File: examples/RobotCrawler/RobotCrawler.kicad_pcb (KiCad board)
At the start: 2 copper layers, 50 x 40 mm, 55 parts

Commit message: floorplanned
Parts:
- removed rgb_tp: 5015 (Keystone) - _mcu_gpio_rgb_link, edg:TestPoint_TE_RCT_0805
- removed tp_1v2: 5015 (Keystone) - v1v2, edg:TestPoint_TE_RCT_0805
- removed tp_2v5: 5015 (Keystone) - v2v5, edg:TestPoint_TE_RCT_0805
- moved reg_2v5.ic 140.7 mm to (163.0, 65.0)
- moved reg_2v5.in_cap 140.7 mm to (163.0, 62.0)
- moved reg_2v5.out_cap 140.7 mm to (163.0, 68.0)
- moved rgbs.led[3] 122.8 mm to (163.0, 76.0)
- moved rgbs.led[2] 122.6 mm to (163.0, 72.0)
- moved cam.reset_pull 120.2 mm to (156.0, 73.0), turned to 90 degrees
- moved reg_1v2.ic 116.7 mm to (137.0, 65.0)
- moved reg_1v2.in_cap 116.7 mm to (137.0, 62.0)
- moved reg_1v2.out_cap 116.7 mm to (137.0, 68.0)
- moved cam.dovdd_cap 116.6 mm to (150.0, 73.0), turned to -90 degrees
- moved cam.pclk_cap 116.6 mm to (147.0, 73.0), turned to -90 degrees
- moved cam.reset_cap 116.6 mm to (153.0, 73.0), turned to -90 degrees
- moved cam.device 115.1 mm to (150.0, 64.0)
- moved rgbs.led[0] 100.8 mm to (137.0, 76.0)
- moved rgbs.led[1] 98.4 mm to (137.0, 72.0)
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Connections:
- net rgb_tp.io renamed rgbs.din
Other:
- board size 50 x 40 mm -> 50 x 50 mm

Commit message: wip
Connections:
- mcu.ic pad 10: cam.y.9 -> i2c_chain_0.scl
- mcu.ic pad 11: cam.pclk -> servo4.pwm
- mcu.ic pad 12: ledg.signal -> servo3.pwm
- mcu.ic pad 13: cam.xclk -> cam.vsync
- mcu.ic pad 15: servo3.fb -> cam.y.9
- mcu.ic pad 17: ledb.signal -> cam.xclk
- mcu.ic pad 18: cam.y.2 -> cam.y.8
- mcu.ic pad 19: cam.y.3 -> cam.y.7
- mcu.ic pad 20: cam.y.4 -> cam.pclk
- mcu.ic pad 21: cam.y.5 -> cam.y.6
- mcu.ic pad 22: cam.y.6 -> cam.y.2
- mcu.ic pad 23: cam.vsync -> cam.y.5
- mcu.ic pad 24: servo2.pwm -> cam.y.3
- mcu.ic pad 25: servo1.pwm -> cam.y.4
- mcu.ic pad 31: servo3.pwm -> servo1.pwm
- mcu.ic pad 32: servo4.pwm -> servo2.pwm
- mcu.ic pad 33: rgbs.din -> ledr.signal
- mcu.ic pad 34: (no net) -> ledg.signal
- mcu.ic pad 35: (no net) -> ledb.signal
- mcu.ic pad 38: servo2.fb -> rgbs.din
- mcu.ic pad 39: servo1.fb -> (no net)
- mcu.ic pad 4: servo4.fb -> servo1.fb
- mcu.ic pad 5: i2c_chain_0.scl -> servo2.fb
- mcu.ic pad 6: i2c_chain_0.sda -> servo3.fb
- mcu.ic pad 7: ledr.signal -> servo4.fb
- mcu.ic pad 8: cam.y.7 -> (no net)
- mcu.ic pad 9: cam.y.8 -> i2c_chain_0.sda
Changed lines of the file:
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@@
       (net 11 "mcu.program_en_node"))
     (pad "4" smd rect (at -8.75 -1.45 180) (size 1.5 0.9) (layers "F.Cu" "F.Paste" "F.Mask")
+      (net 38 "servo1.fb"))
+    (pad "5" smd rect (at -8.75 -0.18 180) (size 1.5 0.9) (layers "F.Cu" "F.Paste" "F.Mask")
+      (net 37 "servo2.fb"))
+    (pad "6" smd rect (at -8.75 1.09 180) (size 1.5 0.9) (layers "F.Cu" "F.Paste" "F.Mask")
+      (net 22 "servo3.fb"))
+    (pad "7" smd rect (at -8.75 2.36 180) (size 1.5 0.9) (layers "F.Cu" "F.Paste" "F.Mask")
       (net 13 "servo4.fb"))
-    (pad "5" smd rect (at -8.75 -0.18 180) (size 1.5 0.9) (layers "F.Cu" "F.Paste" "F.Mask")
+    (pad "8" smd rect (at -8.75 3.63 180) (size 1.5 0.9) (layers "F.Cu" "F.Paste" "F.Mask"))
+    (pad "9" smd rect (at -8.75 4.9 180) (size 1.5 0.9) (layers "F.Cu" "F.Paste" "F.Mask")
+      (net 3 "i2c_chain_0.sda"))
+    (pad "10" smd rect (at -8.75 6.17 180) (size 1.5 0.9) (layers "F.Cu" "F.Paste" "F.Mask")
       (net 5 "i2c_chain_0.scl"))
-    (pad "6" smd rect (at -8.75 1.09 180) (size 1.5 0.9) (layers "F.Cu" "F.Paste" "F.Mask")
-      (net 3 "i2c_chain_0.sda"))
-    (pad "7" smd rect (at -8.75 2.36 180) (size 1.5 0.9) (layers "F.Cu" "F.Paste" "F.Mask")
-      (net 14 "ledr.signal"))
-    (pad "8" smd rect (at -8.75 3.63 180) (size 1.5 0.9) (layers "F.Cu" "F.Paste" "F.Mask")
-      (net 15 "cam.y.7"))
-    (pad "9" smd rect (at -8.75 4.9 180) (size 1.5 0.9) (layers "F.Cu" "F.Paste" "F.Mask")
-      (net 16 "cam.y.8"))
-    (pad "10" smd rect (at -8.75 6.17 180) (size 1.5 0.9) (layers "F.Cu" "F.Paste" "F.Mask")
-      (net 17 "cam.y.9"))
     (pad "11" smd rect (at -8.75 7.44 180) (size 1.5 0.9) (layers "F.Cu" "F.Paste" "F.Mask")
-      (net 18 "cam.pclk"))
+      (net 34 "servo4.pwm"))
     (pad "12" smd rect (at -8.75 8.71 180) (size 1.5 0.9) (layers "F.Cu" "F.Paste" "F.Mask")
-      (net 19 "ledg.signal"))
+      (net 33 "servo3.pwm"))
     (pad "13" smd rect (at -8.75 9.98 180) (size 1.5 0.9) (layers "F.Cu" "F.Paste" "F.Mask")
-      (net 20 "cam.xclk"))
+      (net 29 "cam.vsync"))
     (pad "14" smd rect (at -8.75 11.25) (size 1.5 0.9) (layers "F.Cu" "F.Paste" "F.Mask")
       (net 21 "cam.href"))
     (pad "15" smd rect (at -6.985 12.5 90) (size 1.5 0.9) (layers "F.Cu" "F.Paste" "F.Mask")
-      (net 22 "servo3.fb"))
+      (net 17 "cam.y.9"))
     (pad "16" smd rect (at -5.715 12.5 90) (size 1.5 0.9) (layers "F.Cu" "F.Paste" "F.Mask"))
     (pad "17" smd rect (at -4.445 12.5 90) (size 1.5 0.9) (layers "F.Cu" "F.Paste" "F.Mask")
-      (net 23 "ledb.signal"))
+      (net 20 "cam.xclk"))
     (pad "18" smd rect (at -3.175 12.5 90) (size 1.5 0.9) (layers "F.Cu" "F.Paste" "F.Mask")
+      (net 16 "cam.y.8"))
+    (pad "19" smd rect (at -1.905 12.5 90) (size 1.5 0.9) (layers "F.Cu" "F.Paste" "F.Mask")
+      (net 15 "cam.y.7"))
+    (pad "20" smd rect (at -0.635 12.5 90) (size 1.5 0.9) (layers "F.Cu" "F.Paste" "F.Mask")
+      (net 18 "cam.pclk"))
+    (pad "21" smd rect (at 0.635 12.5 90) (size 1.5 0.9) (layers "F.Cu" "F.Paste" "F.Mask")
+      (net 28 "cam.y.6"))
+    (pad "22" smd rect (at 1.905 12.5 90) (size 1.5 0.9) (layers "F.Cu" "F.Paste" "F.Mask")
       (net 24 "cam.y.2"))
-    (pad "19" smd rect (at -1.905 12.5 90) (size 1.5 0.9) (layers "F.Cu" "F.Paste" "F.Mask")
+    (pad "23" smd rect (at 3.175 12.5 90) (size 1.5 0.9) (layers "F.Cu" "F.Paste" "F.Mask")
+      (net 27 "cam.y.5"))
+    (pad "24" smd rect (at 4.445 12.5 90) (size 1.5 0.9) (layers "F.Cu" "F.Paste" "F.Mask")
       (net 25 "cam.y.3"))
-    (pad "20" smd rect (at -0.635 12.5 90) (size 1.5 0.9) (layers "F.Cu" "F.Paste" "F.Mask")
+    (pad "25" smd rect (at 5.715 12.5 90) (size 1.5 0.9) (layers "F.Cu" "F.Paste" "F.Mask")
       (net 26 "cam.y.4"))
-    (pad "21" smd rect (at 0.635 12.5 90) (size 1.5 0.9) (layers "F.Cu" "F.Paste" "F.Mask")
-      (net 27 "cam.y.5"))
-    (pad "22" smd rect (at 1.905 12.5 90) (size 1.5 0.9) (layers "F.Cu" "F.Paste" "F.Mask")
-      (net 28 "cam.y.6"))
-    (pad "23" smd rect (at 3.175 12.5 90) (size 1.5 0.9) (layers "F.Cu" "F.Paste" "F.Mask")
-      (net 29 "cam.vsync"))
-    (pad "24" smd rect (at 4.445 12.5 90) (size 1.5 0.9) (layers "F.Cu" "F.Paste" "F.Mask")
-      (net 30 "servo2.pwm"))
-    (pad "25" smd rect (at 5.715 12.5 90) (size 1.5 0.9) (layers "F.Cu" "F.Paste" "F.Mask")
-      (net 31 "servo1.pwm"))
     (pad "26" smd rect (at 6.985 12.5 90) (size 1.5 0.9) (layers "F.Cu" "F.Paste" "F.Mask"))
     (pad "27" smd rect (at 8.75 11.25 180) (size 1.5 0.9) (layers "F.Cu" "F.Paste" "F.Mask")
@@
     (pad "30" smd rect (at 8.75 7.44 180) (size 1.5 0.9) (layers "F.Cu" "F.Paste" "F.Mask"))
     (pad "31" smd rect (at 8.75 6.17 180) (size 1.5 0.9) (layers "F.Cu" "F.Paste" "F.Mask")
-      (net 33 "servo3.pwm"))
+      (net 31 "servo1.pwm"))
     (pad "32" smd rect (at 8.75 4.9 180) (size 1.5 0.9) (layers "F.Cu" "F.Paste" "F.Mask")
-      (net 34 "servo4.pwm"))
+      (net 30 "servo2.pwm"))
     (pad "33" smd rect (at 8.75 3.63 180) (size 1.5 0.9) (layers "F.Cu" "F.Paste" "F.Mask")
-      (net 51 "rgbs.din"))
-    (pad "34" smd rect (at 8.75 2.36 180) (size 1.5 0.9) (layers "F.Cu" "F.Paste" "F.Mask"))
-    (pad "35" smd rect (at 8.75 1.09 180) (size 1.5 0.9) (layers "F.Cu" "F.Paste" "F.Mask"))
+      (net 14 "ledr.signal"))
+    (pad "34" smd rect (at 8.75 2.36 180) (size 1.5 0.9) (layers "F.Cu" "F.Paste" "F.Mask")
+      (net 19 "ledg.signal"))
+    (pad "35" smd rect (at 8.75 1.09 180) (size 1.5 0.9) (layers "F.Cu" "F.Paste" "F.Mask")
+      (net 23 "ledb.signal"))
     (pad "36" smd rect (at 8.75 -0.18 180) (size 1.5 0.9) (layers "F.Cu" "F.Paste" "F.Mask")
       (net 35 "mcu.program_uart_node.b_tx"))
@@
       (net 36 "mcu.program_uart_node.a_tx"))
     (pad "38" smd rect (at 8.75 -2.72 180) (size 1.5 0.9) (layers "F.Cu" "F.Paste" "F.Mask")
-      (net 37 "servo2.fb"))
-    (pad "39" smd rect (at 8.75 -3.99 180) (size 1.5 0.9) (layers "F.Cu" "F.Paste" "F.Mask")
-      (net 38 "servo1.fb"))
+      (net 51 "rgbs.din"))
+    (pad "39" smd rect (at 8.75 -3.99 180) (size 1.5 0.9) (layers "F.Cu" "F.Paste" "F.Mask"))
     (pad "40" smd rect (at 8.75 -5.26 180) (size 1.5 0.9) (layers "F.Cu" "F.Paste" "F.Mask")
       (net 1 "gnd"))

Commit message: improvements to help routing
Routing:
- net mcu.program_uart_node.b_tx: track 0.00 -> 3.78 mm
- net mcu.program_uart_node.a_tx: track 0.00 -> 3.78 mm
- net gnd: track 0.00 -> 2.99 mm
- net v3v3: track 0.00 -> 2.88 mm
- net mcu.program_boot_node: track 0.00 -> 2.88 mm
- net mcu.program_en_node: track 0.00 -> 2.84 mm
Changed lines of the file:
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@@
     (fp_arc (start 0.62074 1.407352) (mid 0.5 1.499999) (end 0.37926 1.407352)
       (stroke (width 0.16) (type solid)) (layer "B.Cu"))
-    (fp_arc (start 0.763205 0.913443) (mid 0.969128 0.866757) (end 1.178844 0.891296)
+    (fp_arc (start 0.763205 0.913443) (mid 0.969127 0.866756) (end 1.178844 0.891296)
       (stroke (width 0.16) (type solid)) (layer "B.Cu"))
     (fp_arc (start 0.820058 -1.56145) (mid 0.75756 -1.62395) (end 0.820058 -1.68645)
@@
     (fp_arc (start 0.820058 -1.43645) (mid 0.75756 -1.49895) (end 0.820058 -1.56145)
       (stroke (width 0.16) (type solid)) (layer "B.Cu"))
-    (fp_arc (start 0.869178 1.169286) (mid 1.000175 1.003685) (end 1.178836 0.891151)
+    (fp_arc (start 0.869178 1.169286) (mid 1.000175 1.003686) (end 1.178836 0.891151)
       (stroke (width 0.16) (type solid)) (layer "B.Cu"))
     (fp_arc (start 1.093749 -1.89443) (mid 0.000001 2.187499) (end -1.09375 -1.894429)
@@
     (style (thickness 0.1) (arrow_length 1.27) (text_position_mode 0) (extension_height 0.58642) (extension_offset 0.5) keep_text_aligned)
   )
+  (segment (start 135 106.905) (end 135 109) (width 0.3) (layer "F.Cu") (net 1))
+  (segment (start 134.365 106.27) (end 135 106.905) (width 0.3) (layer "F.Cu") (net 1))
+  (segment (start 135.635 106.27) (end 136.030416 106.27) (width 0.15) (layer "F.Cu") (net 11))
+  (segment (start 136.030416 106.27) (end 137.760416 108) (width 0.15) (layer "F.Cu") (net 11))
+  (segment (start 134.365 103.73) (end 134.1007 103.4657) (width 0.3) (layer "F.Cu") (net 12))
+  (segment (start 134.1007 101.1007) (end 134 101) (width 0.3) (layer "F.Cu") (net 12))
+  (segment (start 134.1007 103.4657) (end 134.1007 101.1007) (width 0.3) (layer "F.Cu") (net 12))
+  (segment (start 136 103.365) (end 136 101) (width 0.15) (layer "F.Cu") (net 32))
+  (segment (start 135.635 103.73) (end 136 103.365) (width 0.15) (layer "F.Cu") (net 32))
+  (segment (start 136.635 104) (end 139 104) (width 0.15) (layer "F.Cu") (net 35))
+  (segment (start 135.635 105) (end 136.635 104) (width 0.15) (layer "F.Cu") (net 35))
+  (segment (start 134.365 105) (end 133.365 104) (width 0.15) (layer "F.Cu") (net 36))
+  (segment (start 133.365 104) (end 131 104) (width 0.15) (layer "F.Cu") (net 36))
   (zone (net 1) (net_name "gnd") (layers "F&B.Cu") (hatch edge 0.508)
     (connect_pads (clearance 0.254))

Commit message: Update RobotCrawler.kicad_pcb
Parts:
- moved cam.device 18.0 mm to (150.0, 82.0)
- moved reg_2v5.in_cap 15.7 mm to (156.0, 76.0), turned to -90 degrees
- moved rgbs.led[0] 14.6 mm to (141.0, 62.0)
- moved rgbs.led[3] 14.6 mm to (159.0, 62.0)
- moved rgbs.led[1] 14.1 mm to (147.0, 62.0)
- moved rgbs.led[2] 14.1 mm to (153.0, 62.0)
- moved reg_1v2.in_cap 14.0 mm to (138.0, 76.0), turned to 90 degrees
- moved compass.c1 14.0 mm to (155.0, 67.0)
- moved compass.ic 14.0 mm to (150.0, 66.0)
- moved compass.set_cap 14.0 mm to (155.0, 65.0)
- moved compass.vdd_cap 14.0 mm to (145.0, 65.0)
- moved i2c_pull.scl_res 14.0 mm to (145.0, 67.0)
- moved i2c_pull.sda_res 14.0 mm to (145.0, 69.0)
- moved imu.ic 14.0 mm to (150.0, 71.0)
- moved imu.vdd_cap 14.0 mm to (155.0, 71.0)
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
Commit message: layout round 2
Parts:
- turned C10 to -90 degrees
- turned C15 to 90 degrees
- turned C16 to 90 degrees
- turned C17 to 90 degrees
- turned R7 to -90 degrees
- renumbered imu.vdd_cap to C1, reg_1v2.in_cap to C10, reg_1v2.out_cap to C11, mcu.vcc_cap0 to C12, mcu.vcc_cap1 to C13, mcu.en_pull.c to C14, cam.dovdd_cap to C15, cam.pclk_cap to C16, cam.reset_cap to C17, imu.vddio_cap to C2, compass.vdd_cap to C3, compass.set_cap to C4, compass.c1 to C5, reg_3v3.in_cap to C6, reg_3v3.out_cap to C7, reg_2v5.in_cap to C8, reg_2v5.out_cap to C9, ledr.package to D1, ledg.package to D2, ledb.package to D3, rgbs.led[0] to D4, rgbs.led[1] to D5, rgbs.led[2] to D6, rgbs.led[3] to D7, batt to J1, servo1 to J2, servo2 to J3, servo3 to J4, servo4 to J5, mcu.prog to J6, cam.device to J7, mcu.en_pull.r to R1, i2c_pull.scl_res to R2, i2c_pull.sda_res to R3, ledr.res to R4, ledg.res to R5, ledb.res to R6, cam.reset_pull to R7, tp_vbatt to TP1, tp_gnd to TP2, tp_3v3 to TP3, i2c_tp.tp_scl to TP4, i2c_tp.tp_sda to TP5, imu.ic to U1, compass.ic to U2, reg_3v3.ic to U3, reg_2v5.ic to U4, reg_1v2.ic to U5, mcu.ic to U6

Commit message: Update RobotCrawler.kicad_pcb
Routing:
- net mcu.program_uart_node.a_tx: track 3.78 -> 0.00 mm
- net mcu.program_en_node: track 2.84 -> 0.00 mm
- net gnd: track 2.99 -> 2.05 mm
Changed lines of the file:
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@@
     (fp_arc (start 0.62074 1.407352) (mid 0.5 1.499999) (end 0.37926 1.407352)
       (stroke (width 0.16) (type solid)) (layer "B.Cu"))
-    (fp_arc (start 0.763205 0.913443) (mid 0.969127 0.866758) (end 1.178844 0.891296)
+    (fp_arc (start 0.763205 0.913443) (mid 0.969128 0.866757) (end 1.178844 0.891296)
       (stroke (width 0.16) (type solid)) (layer "B.Cu"))
     (fp_arc (start 0.820058 -1.56145) (mid 0.75756 -1.62395) (end 0.820058 -1.68645)
@@
     (fp_arc (start 0.820058 -1.43645) (mid 0.75756 -1.49895) (end 0.820058 -1.56145)
       (stroke (width 0.16) (type solid)) (layer "B.Cu"))
-    (fp_arc (start 0.869178 1.169286) (mid 1.000176 1.003686) (end 1.178836 0.891151)
+    (fp_arc (start 0.869178 1.169286) (mid 1.000175 1.003684) (end 1.178836 0.891151)
       (stroke (width 0.16) (type solid)) (layer "B.Cu"))
     (fp_arc (start 1.093749 -1.89443) (mid 0.000001 2.187499) (end -1.09375 -1.894429)
@@
     (style (thickness 0.1) (arrow_length 1.27) (text_position_mode 0) (extension_height 0.58642) (extension_offset 0.5) keep_text_aligned)
   )
-  (segment (start 135 106.905) (end 135 109) (width 0.3) (layer "F.Cu") (net 1))
-  (segment (start 134.365 106.27) (end 135 106.905) (width 0.3) (layer "F.Cu") (net 1))
-  (segment (start 135.635 106.27) (end 136.030416 106.27) (width 0.15) (layer "F.Cu") (net 11))
-  (segment (start 136.030416 106.27) (end 137.760416 108) (width 0.15) (layer "F.Cu") (net 11))
+  (segment (start 134.052908 106.27) (end 132.822908 107.5) (width 0.2) (layer "F.Cu") (net 1))
+  (segment (start 134.365 106.27) (end 134.052908 106.27) (width 0.2) (layer "F.Cu") (net 1))
   (segment (start 134.365 103.73) (end 134.1007 103.4657) (width 0.3) (layer "F.Cu") (net 12))
-  (segment (start 134.1007 101.1007) (end 134 101) (width 0.3) (layer "F.Cu") (net 12))
   (segment (start 134.1007 103.4657) (end 134.1007 101.1007) (width 0.3) (layer "F.Cu") (net 12))
   (segment (start 136 103.365) (end 136 101) (width 0.15) (layer "F.Cu") (net 32))
@@
   (segment (start 136.635 104) (end 139 104) (width 0.15) (layer "F.Cu") (net 35))
   (segment (start 135.635 105) (end 136.635 104) (width 0.15) (layer "F.Cu") (net 35))
-  (segment (start 134.365 105) (end 133.365 104) (width 0.15) (layer "F.Cu") (net 36))
-  (segment (start 133.365 104) (end 131 104) (width 0.15) (layer "F.Cu") (net 36))
   (zone (net 1) (net_name "gnd") (layers "F&B.Cu") (hatch edge 0.508)
     (connect_pads (clearance 0.254))

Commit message: Update RobotCrawler.kicad_pcb
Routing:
- net mcu.program_uart_node.a_tx: track 0.00 -> 9.75 mm, vias 0 -> 2
- net mcu.program_uart_node.b_tx: track 3.78 -> 6.01 mm
- net gnd: track 2.05 -> 2.37 mm, vias 0 -> 1
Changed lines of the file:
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@@
   (segment (start 134.052908 106.27) (end 132.822908 107.5) (width 0.2) (layer "F.Cu") (net 1))
   (segment (start 134.365 106.27) (end 134.052908 106.27) (width 0.2) (layer "F.Cu") (net 1))
+  (segment (start 132.822908 107.5) (end 132.5 107.5) (width 0.3) (layer "F.Cu") (net 1))
+  (via (at 132.5 107.5) (size 0.7) (drill 0.3) (layers "F.Cu" "B.Cu") (net 1))
   (segment (start 134.365 103.73) (end 134.1007 103.4657) (width 0.3) (layer "F.Cu") (net 12))
   (segment (start 134.1007 103.4657) (end 134.1007 101.1007) (width 0.3) (layer "F.Cu") (net 12))
   (segment (start 136 103.365) (end 136 101) (width 0.15) (layer "F.Cu") (net 32))
   (segment (start 135.635 103.73) (end 136 103.365) (width 0.15) (layer "F.Cu") (net 32))
-  (segment (start 136.635 104) (end 139 104) (width 0.15) (layer "F.Cu") (net 35))
-  (segment (start 135.635 105) (end 136.635 104) (width 0.15) (layer "F.Cu") (net 35))
+  (segment (start 136.51645 104.11855) (end 136.0675 104.5675) (width 0.15) (layer "F.Cu") (net 35))
+  (segment (start 141.25 104.18) (end 141.18855 104.11855) (width 0.15) (layer "F.Cu") (net 35))
+  (segment (start 141.18855 104.11855) (end 136.51645 104.11855) (width 0.15) (layer "F.Cu") (net 35))
+  (segment (start 135.635 105) (end 136.0675 104.5675) (width 0.15) (layer "F.Cu") (net 35))
+  (segment (start 134.365 105) (end 134.365 104.865) (width 0.15) (layer "F.Cu") (net 36))
+  (segment (start 134.365 104.865) (end 133.5 104) (width 0.15) (layer "F.Cu") (net 36))
+  (segment (start 140.05 105.45) (end 140 105.5) (width 0.15) (layer "F.Cu") (net 36))
+  (segment (start 141.25 105.45) (end 140.05 105.45) (width 0.15) (layer "F.Cu") (net 36))
+  (via (at 140 105.5) (size 0.7) (drill 0.3) (layers "F.Cu" "B.Cu") (net 36))
+  (via (at 133.5 104) (size 0.7) (drill 0.3) (layers "F.Cu" "B.Cu") (net 36))
+  (segment (start 133.5 104) (end 138.5 104) (width 0.15) (layer "B.Cu") (net 36))
+  (segment (start 138.5 104) (end 140 105.5) (width 0.15) (layer "B.Cu") (net 36))
   (zone (net 1) (net_name "gnd") (layers "F&B.Cu") (hatch edge 0.508)
     (connect_pads (clearance 0.254))
@@
     (polygon
       (pts
-        (xy 175.5 110.5)
-        (xy 124.5 110.5)
-        (xy 124.5 59.5)
-        (xy 175.5 59.5)
+        (xy 123.5 110)
+        (xy 72.5 110)
+        (xy 72.5 59)
+        (xy 123.5 59)
       )
     )

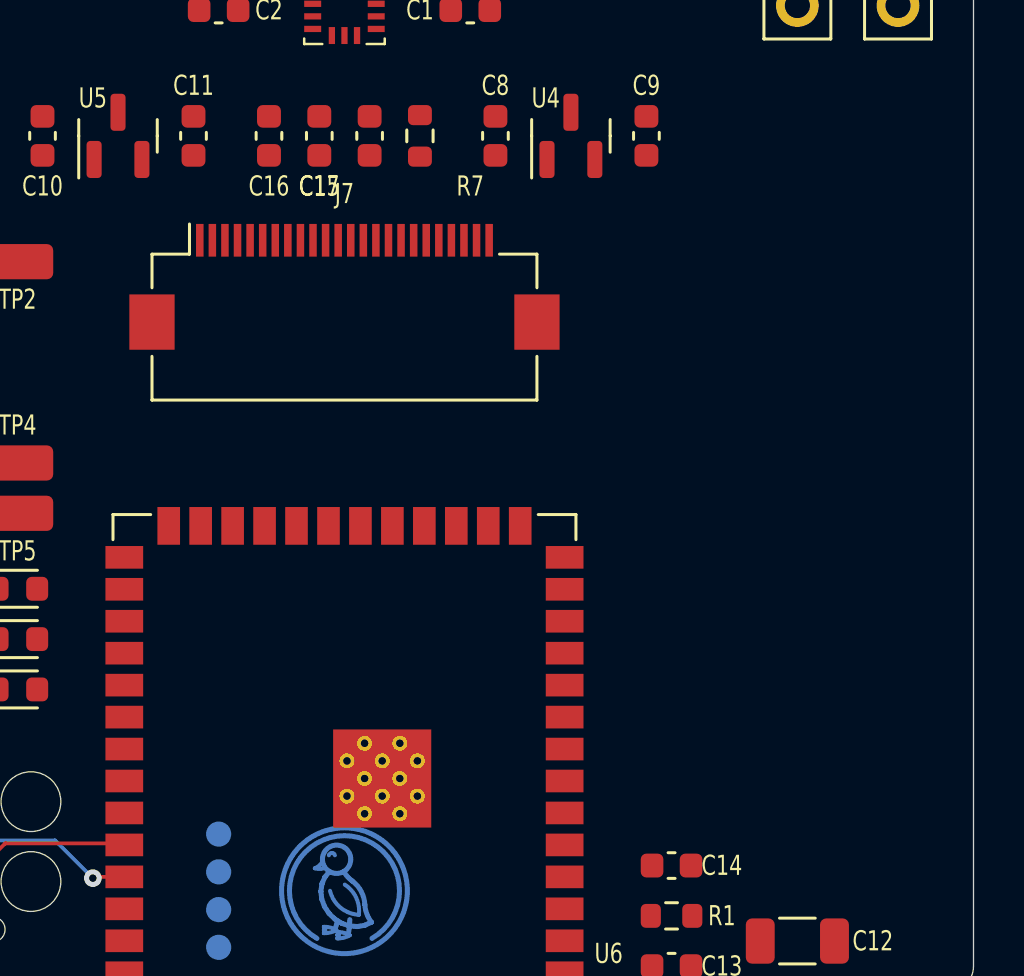
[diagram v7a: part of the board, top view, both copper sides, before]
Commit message: add a oled
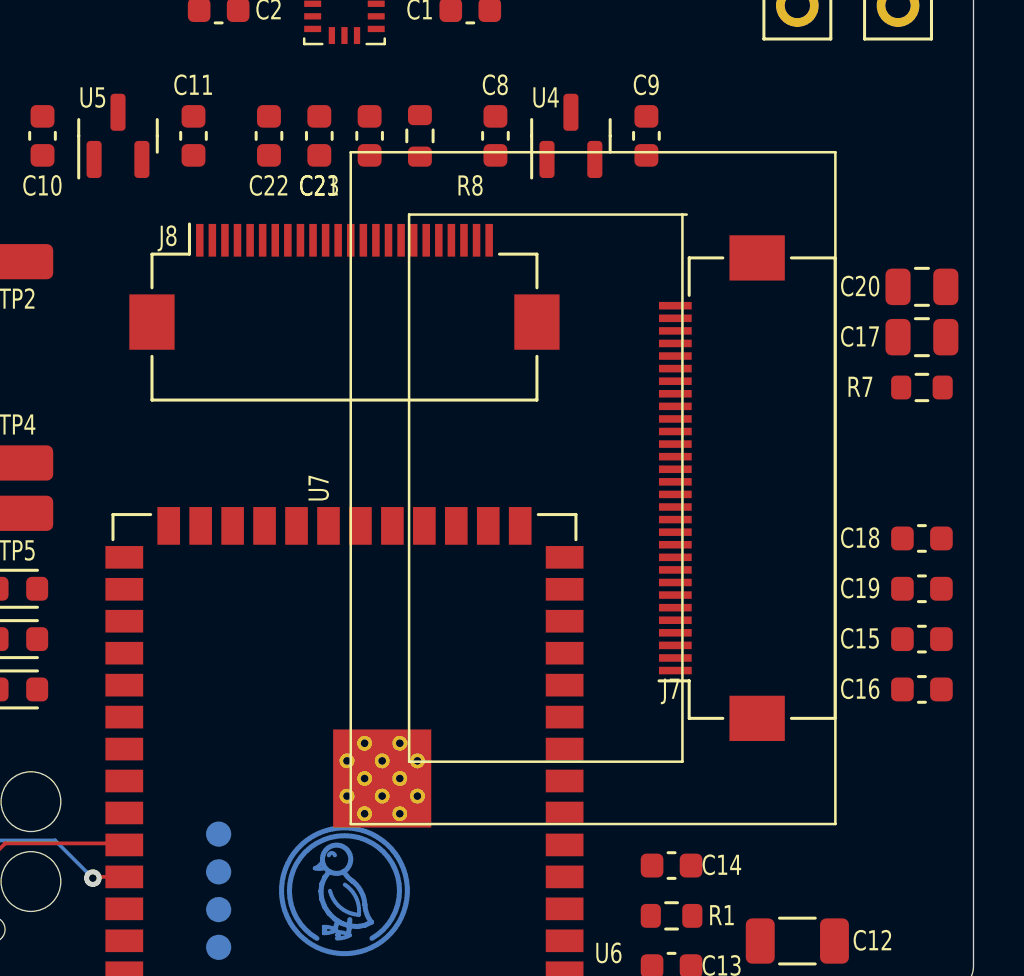
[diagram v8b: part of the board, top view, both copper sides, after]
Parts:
- added C15: 1uF, Capacitor_SMD:C_0603_1608Metric, F.Cu at (172.9, 96.0)
- added C16: 1uF, Capacitor_SMD:C_0603_1608Metric, F.Cu at (172.9, 98.0)
- added C17: 4.7uF, Capacitor_SMD:C_0805_2012Metric, F.Cu at (172.9, 84.0)
- added C18: 1uF, Capacitor_SMD:C_0603_1608Metric, F.Cu at (172.9, 92.0)
- added C19: 1uF, Capacitor_SMD:C_0603_1608Metric, F.Cu at (172.9, 94.0)
- added C20: 2.2uF, Capacitor_SMD:C_0805_2012Metric, F.Cu at (172.9, 82.0)
- added J7: FH12-30S-0.5SH (Hirose), Connector_FFC-FPC:Hirose_FH12-30S-0.5SH_1x30-1MP_P0.50mm_Horizontal, F.Cu at (165.0, 90.0)
- added R7: 390k, 1%, 0.1 W, Resistor_SMD:R_0603_1608Metric, F.Cu at (172.9, 86.0)
- added U7: ER-OLED-0.96-1.1 (EastRising), edg:Lcd_Er_Oled0.96_1.1_Outline, F.Cu at (158.0, 90.0)
- renumbered C15 to C21, C16 to C22, C17 to C23, J7 to J8, R7 to R8
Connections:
- U6 pad 39: (no net) -> oled.reset
